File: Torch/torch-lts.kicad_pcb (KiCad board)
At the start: 2 copper layers, 99.6 x 99.6 mm, 18 parts, among them SW1 SW_SPDT

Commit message: update for BSidesKC
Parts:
- added REF**: 1x2, Connector_PinHeader_2.54mm:PinHeader_1x02_P2.54mm_Vertical, B.Cu at (172.3, 138.2)
- BT1: footprint BadgePirates:BatteryHolder_MPD_BC2003_1x2032_Fixed -> BadgePirates:2032 Through Hold Holder
- SW1: value SW_SPDT -> Push Button; footprint BadgePirates:SW_Slide_1P2T_CK_TH -> BadgePirates:SW_PUSH_6mm_H5mm
- moved G*** 41.9 mm to (130.6, 91.9)
- moved G*** 23.5 mm to (95.0, 72.0)
- moved SW1 21.2 mm to (141.8, 100.1)
- moved BT1 19.5 mm to (125.0, 91.4), turned to 45 degrees
- moved R1 12.1 mm to (151.4, 119.3)
- moved G*** 11.7 mm to (147.3, 112.1)
- moved G*** 0.47 mm to (161.4, 122.6)
- moved G*** 0.34 mm to (153.2, 130.4)
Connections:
- BT1 pad 1: Net-(BT1-Pad1) -> Net-(BT1-+)
- R1 pad 1: Net-(R1-Pad1) -> Net-(SW1A-D)
- SW1 pad 1: Net-(R1-Pad1) -> Net-(BT1-+)
- SW1 pad 2: Net-(BT1-Pad1) -> Net-(SW1A-D)
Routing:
- net Net-(BT1-Pad1): track 48.6 -> 0.00 mm
- net Net-(BT1-+): track 0.00 -> 45.4 mm
- net Net-(R1-Pad1): track 40.5 -> 0.00 mm
- net Net-(SW1A-D): track 0.00 -> 25.2 mm
- net VCC: track 33.0 -> 13.6 mm
- net GND: vias 4 -> 0
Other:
- outline, holes or cut-outs redrawn
- board text added: "Step 1 Solder on Battery Connector Step 2 Solder Each Resistor (direction doesn't matter) Step 3 Solder Each Button (direction doesn't matter) Step 4 Solder on Each LED (Direction Matters!)*"

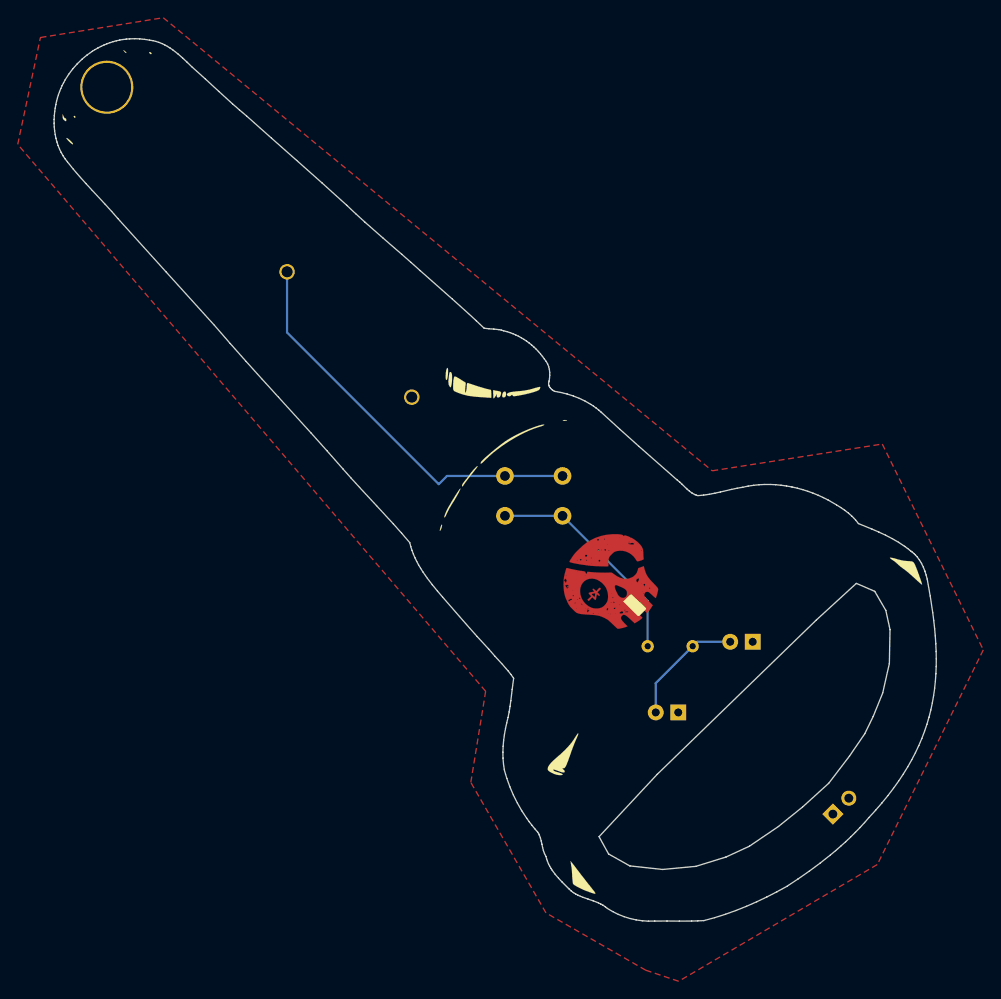
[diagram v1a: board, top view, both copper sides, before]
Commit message: updated Logos and Adjusted size of res, alighted footprints properly to board
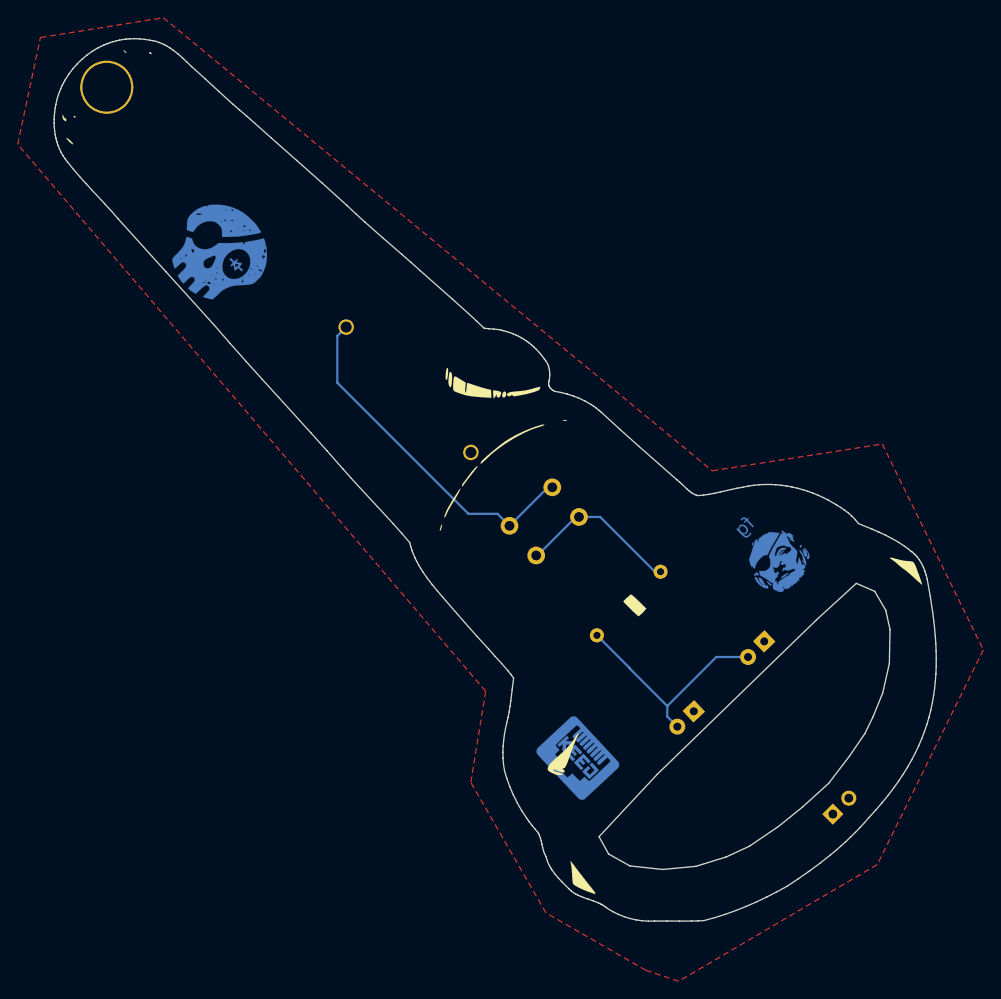
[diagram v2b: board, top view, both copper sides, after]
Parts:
- removed the G*** at (142.0, 120.9)
- removed the G*** at (130.6, 91.9)
- removed R1: R_US, Resistor_THT:R_Axial_DIN0204_L3.6mm_D1.6mm_P5.08mm_Horizontal
- added G***: NG_BSilk_B.Cu, BadgePiratesLogos:NG_B.Cu, F.Cu at (143.6, 131.7)
- added G***: fg, BadgePiratesLogos:FG_B.Cu, F.Cu at (165.8, 109.5)
- added Resister: R_US, Resistor_THT:R_Axial_DIN0207_L6.3mm_D2.5mm_P10.16mm_Horizontal, B.Cu at (152.8, 110.9)
- BT1: value Battery_Cell -> Battery
- Button: renamed from SW1; value Push Button -> Push ON
- G***: moved to B.Cu
- moved G*** 57.9 mm to (103.0, 74.9), turned to 135 degrees
- moved G*** 9.21 mm to (150.0, 121.8), turned to -140 degrees
- moved BT1 9.14 mm to (131.7, 97.7)
- moved G*** 8.78 mm to (158.2, 114.4), turned to -140 degrees
- moved G*** 6.54 mm to (91.2, 66.7)
- moved D2 1.76 mm to (156.6, 126.6), turned to -137 degrees
- moved Button 1.73 mm to (140.6, 101.4), turned to -138 degrees
- moved D1 1.31 mm to (164.6, 118.8), turned to -136 degrees
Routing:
- net VCC: track 13.6 -> 25.5 mm
- net Net-(SW1A-D): track 25.2 -> 18.4 mm
- net Net-(BT1-+): track 45.4 -> 39.5 mm
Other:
- board text added: "BSidesKC 2023"
- board text added: "Step 1 Solder Resistor (direction doesn't matter) Step 2 Solder Button (direction doesn't matter) Step 3 Solder on Each LED (Direction Matters!)* Step 4 Solder on Battery Connector"
- board text added: "long"
- board text added: "short"
- board text removed: "Step 1 Solder on Battery Connector Step 2 Solder Each Resistor (direction doesn't matter) Step 3 Solder Each Button (direction doesn't matter) Step 4 Solder on Each LED (Direction Matters!)*"
